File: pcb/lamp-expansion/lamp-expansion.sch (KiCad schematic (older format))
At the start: 96 parts, among them IC1 78L50_SOT, IC10 74HC4050, IC2 MCP73811, IC3 AP2411, IC4 LM2623_VSSOP, IC5 LM1117_3.3, IC6 LM1117_5.0, IC7 FT230X_SOP, IC8 TLV1117LV28, IC9 CC3000, J1 MICROUSB, J10 CC-IO, J2 7-15V, J3 SERIAL, J4 5PIN_INPUT, J5 2PIN_POWER, J6 2PIN_IO, J7 2PIN_POWER, J8 AVR_ISP, J9 UF.L, Q1 2N7002

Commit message: kicad bug. building latest revision. hang on
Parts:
- gave numbers to parts that had none: 2
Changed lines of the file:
@@
 $EndComp
 $Comp
-L LED LED?
+L LED LED2
 U 1 1 5355ACEE
 P 5850 9600
-F 0 "LED?" H 6000 9700 60  0000 C CNN
+F 0 "LED2" H 6000 9700 60  0000 C CNN
 F 1 "GRN" H 5700 9700 60  0000 C CNN
 F 2 "" H 5850 9600 60  0001 C CNN
@@
 $EndComp
 $Comp
-L LED LED?
+L LED LED1
 U 1 1 5355AD34
 P 5850 9400
-F 0 "LED?" H 6000 9300 60  0000 C CNN
+F 0 "LED1" H 6000 9300 60  0000 C CNN
 F 1 "YEL" H 5700 9300 60  0000 C CNN
 F 2 "" H 5850 9400 60  0001 C CNN
@@
 	2150 6350 2050 6350
 $Comp
-L GND #PWR056
+L GND #PWR055
 U 1 1 535857C8
 P 2450 6450
-F 0 "#PWR056" H 2450 6450 30  0001 C CNN
+F 0 "#PWR055" H 2450 6450 30  0001 C CNN
 F 1 "GND" H 2450 6380 30  0001 C CNN
 F 2 "" H 2450 6450 60  0000 C CNN
@@
 $EndComp
 $Comp
-L GND #PWR057
+L GND #PWR056
 U 1 1 53585E0F
 P 1350 6750
-F 0 "#PWR057" H 1350 6750 30  0001 C CNN
+F 0 "#PWR056" H 1350 6750 30  0001 C CNN
 F 1 "GND" H 1350 6680 30  0001 C CNN
 F 2 "" H 1350 6750 60  0000 C CNN
@@
 	4550 7100 4550 7250
 $Comp
-L GND #PWR058
+L GND #PWR057
 U 1 1 5358640B
 P 4550 7550
-F 0 "#PWR058" H 4550 7550 30  0001 C CNN
+F 0 "#PWR057" H 4550 7550 30  0001 C CNN
 F 1 "GND" H 4550 7480 30  0001 C CNN
 F 2 "" H 4550 7550 60  0000 C CNN
@@
 $EndComp
 $Comp
-L GND #PWR059
+L GND #PWR058
 U 1 1 535889B6
 P 7600 1650
-F 0 "#PWR059" H 7600 1650 30  0001 C CNN
+F 0 "#PWR058" H 7600 1650 30  0001 C CNN
 F 1 "GND" H 7600 1580 30  0001 C CNN
 F 2 "" H 7600 1650 60  0000 C CNN
@@
 $EndComp
 $Comp
-L GND #PWR060
+L GND #PWR059
 U 1 1 53588CB8
 P 8550 1650
-F 0 "#PWR060" H 8550 1650 30  0001 C CNN
+F 0 "#PWR059" H 8550 1650 30  0001 C CNN
 F 1 "GND" H 8550 1580 30  0001 C CNN
 F 2 "" H 8550 1650 60  0000 C CNN
@@
 $EndComp
 $Comp
-L VCC #PWR061
+L VCC #PWR060
 U 1 1 53588CCC
 P 8550 1550
-F 0 "#PWR061" H 8550 1650 30  0001 C CNN
+F 0 "#PWR060" H 8550 1650 30  0001 C CNN
 F 1 "VCC" H 8550 1650 30  0000 C CNN
 F 2 "" H 8550 1550 60  0000 C CNN
@@
 $EndComp
 $Comp
-L VCC #PWR062
+L VCC #PWR061
 U 1 1 53589C93
 P 8700 3450
-F 0 "#PWR062" H 8700 3550 30  0001 C CNN
+F 0 "#PWR061" H 8700 3550 30  0001 C CNN
 F 1 "VCC" H 8700 3550 30  0000 C CNN
 F 2 "" H 8700 3450 60  0000 C CNN
@@
 $EndComp
 $Comp
-L GND #PWR063
+L GND #PWR062
 U 1 1 53589CA7
 P 9200 3450
-F 0 "#PWR063" H 9200 3450 30  0001 C CNN
+F 0 "#PWR062" H 9200 3450 30  0001 C CNN
 F 1 "GND" H 9200 3380 30  0001 C CNN
 F 2 "" H 9200 3450 60  0000 C CNN
@@
 $EndComp
 $Comp
-L VCC #PWR064
+L VCC #PWR063
 U 1 1 5358A17D
 P 8700 3850
-F 0 "#PWR064" H 8700 3950 30  0001 C CNN
+F 0 "#PWR063" H 8700 3950 30  0001 C CNN
 F 1 "VCC" H 8700 3950 30  0000 C CNN
 F 2 "" H 8700 3850 60  0000 C CNN
@@
 $EndComp
 $Comp
-L GND #PWR065
+L GND #PWR064
 U 1 1 5358A183
 P 9200 3850
-F 0 "#PWR065" H 9200 3850 30  0001 C CNN
+F 0 "#PWR064" H 9200 3850 30  0001 C CNN
 F 1 "GND" H 9200 3780 30  0001 C CNN
 F 2 "" H 9200 3850 60  0000 C CNN
@@
 $EndComp
 $Comp
-L VCC #PWR066
+L VCC #PWR065
 U 1 1 5358A1BC
 P 8700 4250
-F 0 "#PWR066" H 8700 4350 30  0001 C CNN
+F 0 "#PWR065" H 8700 4350 30  0001 C CNN
 F 1 "VCC" H 8700 4350 30  0000 C CNN
 F 2 "" H 8700 4250 60  0000 C CNN
@@
 $EndComp
 $Comp
-L GND #PWR067
+L GND #PWR066
 U 1 1 5358A1C2
 P 9200 4250
-F 0 "#PWR067" H 9200 4250 30  0001 C CNN
+F 0 "#PWR066" H 9200 4250 30  0001 C CNN
 F 1 "GND" H 9200 4180 30  0001 C CNN
 F 2 "" H 9200 4250 60  0000 C CNN
@@
 $EndComp
 $Comp
-L GND #PWR068
+L GND #PWR067
 U 1 1 5358A1F9
 P 7500 4500
-F 0 "#PWR068" H 7500 4500 30  0001 C CNN
+F 0 "#PWR067" H 7500 4500 30  0001 C CNN
 F 1 "GND" H 7500 4430 30  0001 C CNN
 F 2 "" H 7500 4500 60  0000 C CNN
@@
 $EndComp
 $Comp
-L VCC #PWR069
+L VCC #PWR068
 U 1 1 5358A3AE
 P 7500 4600
-F 0 "#PWR069" H 7500 4700 30  0001 C CNN
+F 0 "#PWR068" H 7500 4700 30  0001 C CNN
 F 1 "VCC" H 7500 4700 30  0000 C CNN
 F 2 "" H 7500 4600 60  0000 C CNN
@@
 $EndComp
 $Comp
-L GND #PWR070
+L GND #PWR069
 U 1 1 5358ABD5
 P 7500 4950
-F 0 "#PWR070" H 7500 4950 30  0001 C CNN
+F 0 "#PWR069" H 7500 4950 30  0001 C CNN
 F 1 "GND" H 7500 4880 30  0001 C CNN
 F 2 "" H 7500 4950 60  0000 C CNN
@@
 $EndComp
 $Comp
-L VCC #PWR071
+L VCC #PWR070
 U 1 1 5358ABE2
 P 7500 5050
-F 0 "#PWR071" H 7500 5150 30  0001 C CNN
+F 0 "#PWR070" H 7500 5150 30  0001 C CNN
 F 1 "VCC" H 7500 5150 30  0000 C CNN
 F 2 "" H 7500 5050 60  0000 C CNN
@@
 	12300 2400 12100 2400
 $Comp
-L PWR_FLAG #FLG072
+L PWR_FLAG #FLG071
 U 1 1 53613807
 P 3150 8950
-F 0 "#FLG072" H 3150 9045 30  0001 C CNN
+F 0 "#FLG071" H 3150 9045 30  0001 C CNN
 F 1 "PWR_FLAG" H 3150 9130 30  0000 C CNN
 F 2 "" H 3150 8950 60  0000 C CNN
@@
 $EndComp
 $Comp
-L PWR_FLAG #FLG073
+L PWR_FLAG #FLG072
 U 1 1 53613C3F
 P 5350 7150
-F 0 "#FLG073" H 5350 7245 30  0001 C CNN
+F 0 "#FLG072" H 5350 7245 30  0001 C CNN
 F 1 "PWR_FLAG" H 5350 7330 30  0000 C CNN
 F 2 "" H 5350 7150 60  0000 C CNN
@@
 $EndComp
 $Comp
-L PWR_FLAG #FLG074
+L PWR_FLAG #FLG073
 U 1 1 5361446B
 P 1900 4650
-F 0 "#FLG074" H 1900 4745 30  0001 C CNN
+F 0 "#FLG073" H 1900 4745 30  0001 C CNN
 F 1 "PWR_FLAG" H 1900 4830 30  0000 C CNN
 F 2 "" H 1900 4650 60  0000 C CNN
@@
 Connection ~ 1750 4550
 $Comp
-L PWR_FLAG #FLG075
+L PWR_FLAG #FLG074
 U 1 1 536148A2
 P 2600 4750
-F 0 "#FLG075" H 2600 4845 30  0001 C CNN
+F 0 "#FLG074" H 2600 4845 30  0001 C CNN
 F 1 "PWR_FLAG" H 2600 4930 30  0000 C CNN
 F 2 "" H 2600 4750 60  0000 C CNN

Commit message: fixed typo for 74L05 LDO value
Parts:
- IC1: value 78L50_SOT -> 78L05_SOT
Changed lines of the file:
@@
 P 1750 6450
 F 0 "IC1" H 1900 6050 60  0000 C CNN
-F 1 "78L50_SOT" H 1750 6150 60  0000 C CNN
+F 1 "78L05_SOT" H 1750 6150 60  0000 C CNN
 F 2 "" H 1450 6750 60  0001 C CNN
 F 3 "" H 1550 6850 60  0001 C CNN

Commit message: assign footprints and start layout
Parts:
- removed J2: 7-15V, symbol DCIN
- removed JP1: VBAT-DIR-SELECT, symbol JUMPER_3-PIN-CLOSED
- removed JP2: I-TEST, symbol JUMPER_2-PIN-CLOSED
- removed JP3: MODE-SEL, symbol JUMPER_3-PIN-CLOSED
- added J2: DCIN, symbol DC-BARREL-JACK
- added JP1: VBAT-DIR-SEL, symbol JUMPER_3-PIN
- added JP2: I-TEST, symbol JUMPER_2-PIN
- added JP3: MODE-SEL, symbol JUMPER_3-PIN
- AE1: value ANTENNA -> 2500AT44M0400E; Distrib. Part (none) -> 712-1403-1-ND; Distributor (none) -> Digikey; Manuf. Part (none) -> 2500AT44M0400E; Manufacturer (none) -> Johanson Technology Inc
- F1: value 500mA -> 2A
- IC10: Distrib. Part (none) -> 568-7640-1-ND; Distributor (none) -> Digikey; Manuf. Part (none) -> 74HC4050PW,118; Manufacturer (none) -> NXP Semiconductors
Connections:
- wire segments 279 -> 280
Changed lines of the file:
@@
 P 1900 8950
 F 0 "F1" H 1900 9150 60  0000 C CNN
-F 1 "500mA" H 1900 9050 60  0000 C CNN
+F 1 "2A" H 1900 9050 60  0000 C CNN
 F 2 "" H 1900 8950 60  0000 C CNN
 F 3 "" H 1900 8950 60  0000 C CNN
@@
 DC input and 3.3V LDO
 $Comp
-L DCIN J2
-U 1 1 5355B2AC
-P 1400 4500
-F 0 "J2" H 1350 4250 60  0000 C CNN
-F 1 "7-15V" H 1400 4150 60  0000 C CNN
-F 2 "" H 1400 4500 60  0000 C CNN
-F 3 "" H 1400 4500 60  0000 C CNN
-	1    1400 4500
-	1    0    0    -1
-$EndComp
-$Comp
 L GND #PWR06
 U 1 1 5355B2CA
-P 1750 4650
-F 0 "#PWR06" H 1750 4650 30  0001 C CNN
-F 1 "GND" H 1750 4580 30  0001 C CNN
-F 2 "" H 1750 4650 60  0000 C CNN
-F 3 "" H 1750 4650 60  0000 C CNN
-	1    1750 4650
+P 1750 4750
+F 0 "#PWR06" H 1750 4750 30  0001 C CNN
+F 1 "GND" H 1750 4680 30  0001 C CNN
+F 2 "" H 1750 4750 60  0000 C CNN
+F 3 "" H 1750 4750 60  0000 C CNN
+	1    1750 4750
 	1    0    0    -1
 $EndComp
@@
 	5650 9000 5100 9000
 Wire Wire Line
-	1750 4650 1750 4550
-Wire Wire Line
-	1650 4550 1900 4550
+	1750 4550 1750 4750
 Wire Wire Line
 	3150 4350 3550 4350
@@
 U 1 1 5356B181
 P 1900 4450
-F 0 "D1" H 1950 4650 60  0000 C CNN
-F 1 "MSS2P2" H 2050 4550 60  0000 C CNN
+F 0 "D1" H 1900 4650 60  0000 C CNN
+F 1 "MSS2P2" H 2000 4550 60  0000 C CNN
 F 2 "" H 1650 4450 60  0001 C CNN
 F 3 "" H 1750 4550 60  0001 C CNN
@@
 V_BAT
 Wire Wire Line
-	3300 2850 3600 2850
+	3300 2850 3700 2850
 Wire Wire Line
 	3700 2700 3800 2700
@@
 	12300 3500 12100 3500
 $Comp
-L JUMPER_3-PIN-CLOSED JP1
-U 1 1 535713CB
-P 3700 2850
-F 0 "JP1" V 3600 3300 60  0000 C CNN
-F 1 "VBAT-DIR-SELECT" V 3700 3650 60  0000 C CNN
-F 2 "" H 3550 2850 60  0001 C CNN
-F 3 "" H 3700 2950 60  0001 C CNN
-	1    3700 2850
-	0    1    1    0
-$EndComp
-$Comp
 L JUMPER_2-PIN JP4
 U 1 1 53571425
@@
 	1    0    0    -1
 $EndComp
-$Comp
-L JUMPER_3-PIN-CLOSED JP3
-U 1 1 535718D0
-P 11950 3200
-F 0 "JP3" H 12400 3150 60  0000 C CNN
-F 1 "MODE-SEL" H 12550 3250 60  0000 C CNN
-F 2 "" H 11800 3200 60  0001 C CNN
-F 3 "" H 11950 3300 60  0001 C CNN
-	1    11950 3200
-	-1   0    0    1
-$EndComp
-Wire Wire Line
-	12300 3200 12100 3200
+Wire Wire Line
+	11950 3200 12300 3200
 Wire Wire Line
 	12300 3100 11950 3100
@@
 U 1 1 53573213
 P 12100 1550
-F 0 "AE1" H 12100 1750 60  0000 C CNN
-F 1 "ANTENNA" H 12100 1650 60  0000 C CNN
+F 0 "AE1" H 11650 1750 60  0000 C CNN
+F 1 "2500AT44M0400E" H 11950 1650 60  0000 C CNN
 F 2 "" H 11950 1600 60  0001 C CNN
 F 3 "" H 12100 1700 60  0001 C CNN
+F 4 "Johanson Technology Inc" H 12100 1550 60  0001 C CNN "Manufacturer"
+F 5 "2500AT44M0400E" H 12100 1550 60  0001 C CNN "Manuf. Part"
+F 6 "Digikey" H 12100 1550 60  0001 C CNN "Distributor"
+F 7 "712-1403-1-ND" H 12100 1550 60  0001 C CNN "Distrib. Part"
 	1    12100 1550
 	1    0    0    -1
@@
 F 2 "" H 14150 7400 60  0001 C CNN
 F 3 "" H 14200 7400 60  0001 C CNN
+F 4 "NXP Semiconductors" H 14250 7400 60  0001 C CNN "Manufacturer"
+F 5 "74HC4050PW,118" H 14250 7400 60  0001 C CNN "Manuf. Part"
+F 6 "Digikey" H 14250 7400 60  0001 C CNN "Distributor"
+F 7 "568-7640-1-ND" H 14250 7400 60  0001 C CNN "Distrib. Part"
 	1    14250 7400
 	1    0    0    -1
@@
 Wire Wire Line
 	4550 7550 4550 7450
-$Comp
-L JUMPER_2-PIN-CLOSED JP2
-U 1 1 53586622
-P 4000 6750
-F 0 "JP2" H 4000 6850 60  0000 C CNN
-F 1 "I-TEST" H 4000 6650 60  0000 C CNN
-F 2 "" H 3900 6750 60  0001 C CNN
-F 3 "" H 4000 6850 60  0001 C CNN
-	1    4000 6750
-	1    0    0    -1
-$EndComp
 Wire Wire Line
 	3550 6650 3650 6650
@@
 Connection ~ 3750 6500
 Wire Wire Line
-	3550 6750 3850 6750
+	3550 6750 4250 6750
 Connection ~ 3750 6750
-Wire Wire Line
-	4150 6750 4250 6750
 Wire Wire Line
 	4300 6500 4550 6500
@@
 L PWR_FLAG #FLG073
 U 1 1 5361446B
-P 1900 4650
-F 0 "#FLG073" H 1900 4745 30  0001 C CNN
-F 1 "PWR_FLAG" H 1900 4830 30  0000 C CNN
-F 2 "" H 1900 4650 60  0000 C CNN
-F 3 "" H 1900 4650 60  0000 C CNN
-	1    1900 4650
-	-1   0    0    1
-$EndComp
-Wire Wire Line
-	1900 4550 1900 4650
-Connection ~ 1750 4550
+P 1850 4650
+F 0 "#FLG073" H 1850 4745 30  0001 C CNN
+F 1 "PWR_FLAG" H 1850 4830 30  0000 C CNN
+F 2 "" H 1850 4650 60  0000 C CNN
+F 3 "" H 1850 4650 60  0000 C CNN
+	1    1850 4650
+	0    1    1    0
+$EndComp
 $Comp
 L PWR_FLAG #FLG074
@@
 	0    -1   -1   0
 $EndComp
+$Comp
+L DC-BARREL-JACK J2
+U 1 1 53619F5D
+P 1450 4550
+F 0 "J2" H 1300 4300 60  0000 C CNN
+F 1 "DCIN" H 1350 4200 60  0000 C CNN
+F 2 "" H 1350 4650 60  0000 C CNN
+F 3 "" H 1350 4650 60  0000 C CNN
+	1    1450 4550
+	1    0    0    -1
+$EndComp
+Wire Wire Line
+	1750 4550 1650 4550
+Wire Wire Line
+	1650 4650 1850 4650
+Connection ~ 1750 4650
+$Comp
+L JUMPER_2-PIN JP2
+U 1 1 5361BCCF
+P 4000 6750
+F 0 "JP2" H 4000 6850 60  0000 C CNN
+F 1 "I-TEST" H 4000 6650 60  0000 C CNN
+F 2 "" H 3900 6750 60  0001 C CNN
+F 3 "" H 4000 6850 60  0001 C CNN
+	1    4000 6750
+	1    0    0    -1
+$EndComp
+Connection ~ 4150 6750
+Connection ~ 3850 6750
+$Comp
+L JUMPER_3-PIN JP3
+U 1 1 5361C056
+P 11950 3200
+F 0 "JP3" H 12400 3150 60  0000 C CNN
+F 1 "MODE-SEL" H 12550 3250 60  0000 C CNN
+F 2 "" H 11800 3200 60  0001 C CNN
+F 3 "" H 11950 3300 60  0001 C CNN
+	1    11950 3200
+	-1   0    0    1
+$EndComp
+Wire Wire Line
+	11950 3100 11950 3200
+Connection ~ 12100 3200
+$Comp
+L JUMPER_3-PIN JP1
+U 1 1 5361C257
+P 3700 2850
+F 0 "JP1" V 3650 3300 60  0000 C CNN
+F 1 "VBAT-DIR-SEL" V 3750 3550 60  0000 C CNN
+F 2 "" H 3550 2850 60  0001 C CNN
+F 3 "" H 3700 2950 60  0001 C CNN
+	1    3700 2850
+	0    1    1    0
+$EndComp
+Wire Wire Line
+	3700 2850 3700 2700
+Connection ~ 3600 2850
 $EndSCHEMATC

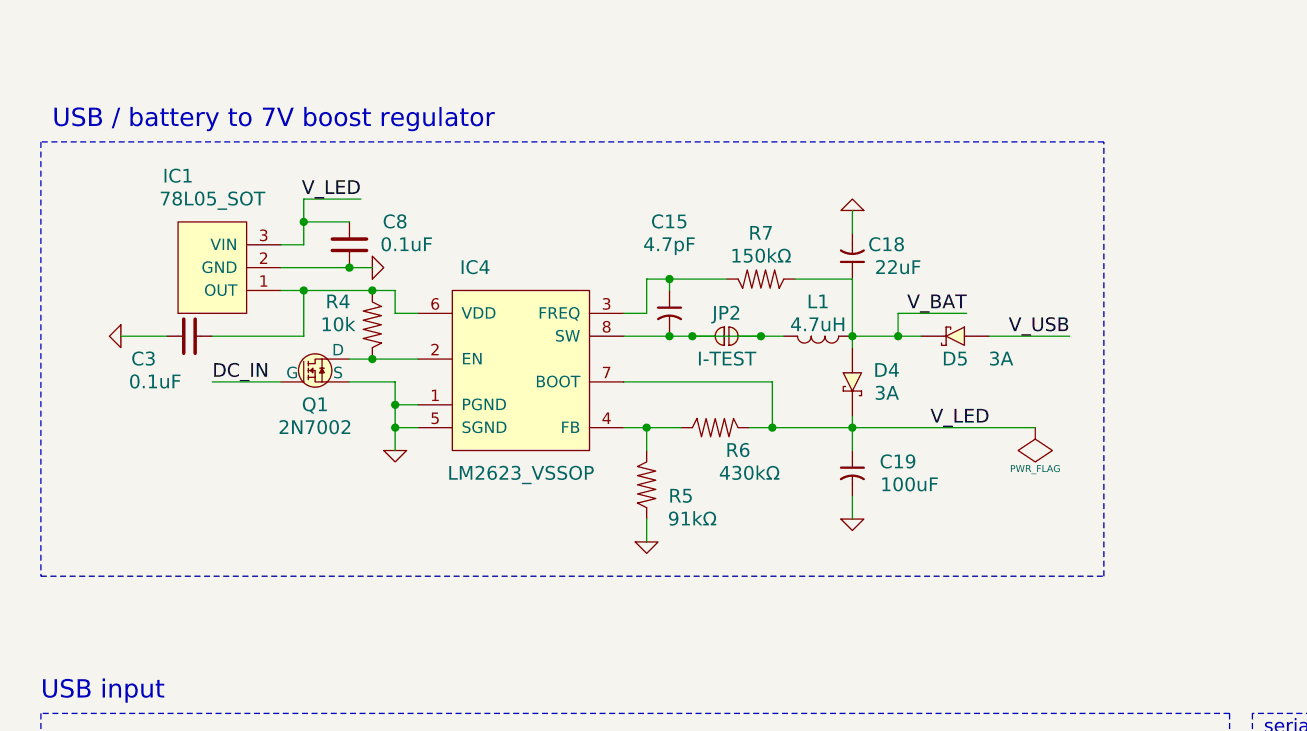
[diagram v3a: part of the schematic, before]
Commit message: replace boost regulator
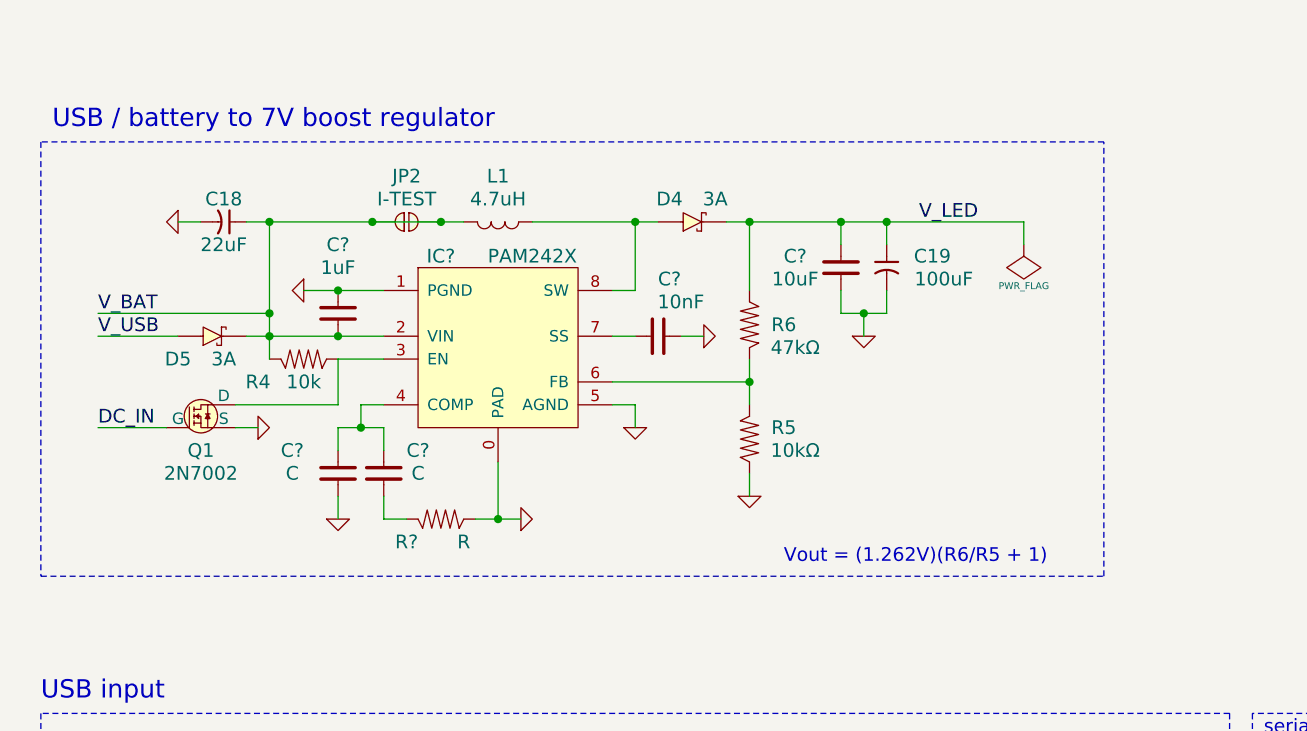
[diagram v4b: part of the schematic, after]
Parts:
- removed C15: 4.7pF, symbol C_POL
- removed C3, C8: 0.1uF, symbol C
- removed IC1: 78L05_SOT, symbol 78LXX_SOT
- removed IC4: LM2623_VSSOP, symbol LM2623_VSSOP
- removed R7: 150kΩ, symbol R
- added C?: 1uF, symbol C
- added C? (x2): C, symbol C
- added C?: 10nF, symbol C
- added C?: 10uF, symbol C
- added IC?: PAM242X, symbol PAM242X
- added R?: R, symbol R
- R5: value 91kΩ -> 10kΩ
- R6: value 430kΩ -> 47kΩ
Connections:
- net GND: now also C?.1, C?.2, C?.2, C?.2, IC?.0 (PAD), IC?.1 (PGND), IC?.5 (AGND), R?.2
- net VCC: now also JP2.1, JP2.2, L1.2, R4.1, C?.2, IC?.2 (VIN); no longer D4.2 (A), L1.1
- net V_LED: now also R6.2, C?.1; no longer R6.1
- net at Q1.3 (D): now also R4.2, IC?.3 (EN); no longer R4.1
- net at R5.1: now also R6.1, IC?.6 (FB); no longer R6.2
- new net: D4.2 (A), IC?.8 (SW), L1.1
- new net: C?.1, C?.1, IC?.4 (COMP)
- new net: C?.1, IC?.7 (SS)
- new net: C?.2, R?.1
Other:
- note added: "Vout = (1.262V)(R6/R5 + 1)"
- moved on the sheet: C18, C19, D4, D5, JP2, L1, Q1, R4, R5, R6

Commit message: boost regulator work
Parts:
- removed C18: 22uF, symbol C_POL
- added C?: 10uF, symbol C
- added C?: 100uF, symbol C_POL
- L1: value 4.7uH -> 6.8uH; Distrib. Part (none) -> SRN6045-6R8YCT-ND; Distributor (none) -> Digikey; Manuf. Part (none) -> SRN6045-6R8Y; Manufacturer (none) -> Bourns Inc
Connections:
- net GND: now also C?.2, C?.2
- net VCC: now also C?.1, C?.1
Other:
- moved on the sheet: BT1, C1, C10, C12, C13, C17, C2, C20, C9, D1, D2, D3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

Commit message: working on the layout;
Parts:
- C18: renamed from C?; value C -> 47pF
- C29: renamed from C?; value C -> 2.2nF
- C30: renamed from C?; value 10nF -> 0.1uF
- IC1: renamed from IC?; value PAM242X -> PAM2421
- R7: renamed from R?; value R -> 51k
- gave numbers to parts that had none: 4
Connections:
- net GND: now also C29.1; no longer R7.2
- net at C18.1, IC1.4 (COMP): now also R7.1; no longer C29.1
- net at C29.2: now also R7.2; no longer R7.1
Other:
- moved on the sheet: C29, R7

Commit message: moving over to main board
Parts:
- removed C11: 0.1uF, symbol C
- IC3: value AP2411 -> AP2401; Distrib. Part AP2411S-13DICT-ND -> AP2401S-13DICT-ND; Manuf. Part AP2411S-13 -> AP2401S-13
